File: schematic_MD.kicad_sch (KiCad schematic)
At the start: 31 parts, among them J1 XT60, J10 Gate_PWR_Jump, J11 CAN_Bus, J13 EXPWR_GND, J2 XT60, J3 XT60, J4 CAN_Bus, J5 Rotaly_encoder_1, J6 Rotaly_encoder_2, J9 Conn_02x01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

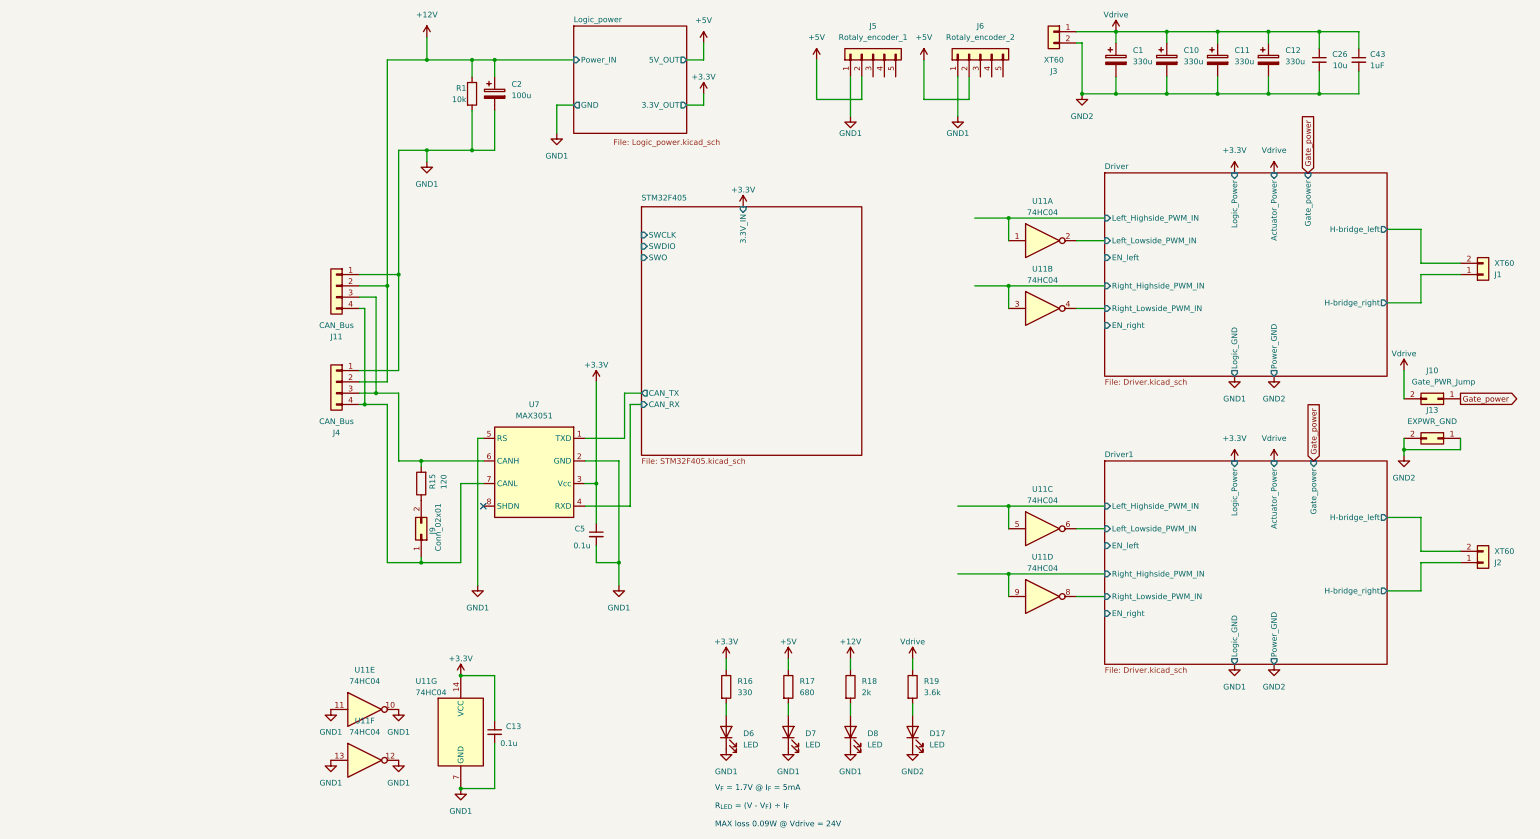
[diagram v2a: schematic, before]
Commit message: logic design update
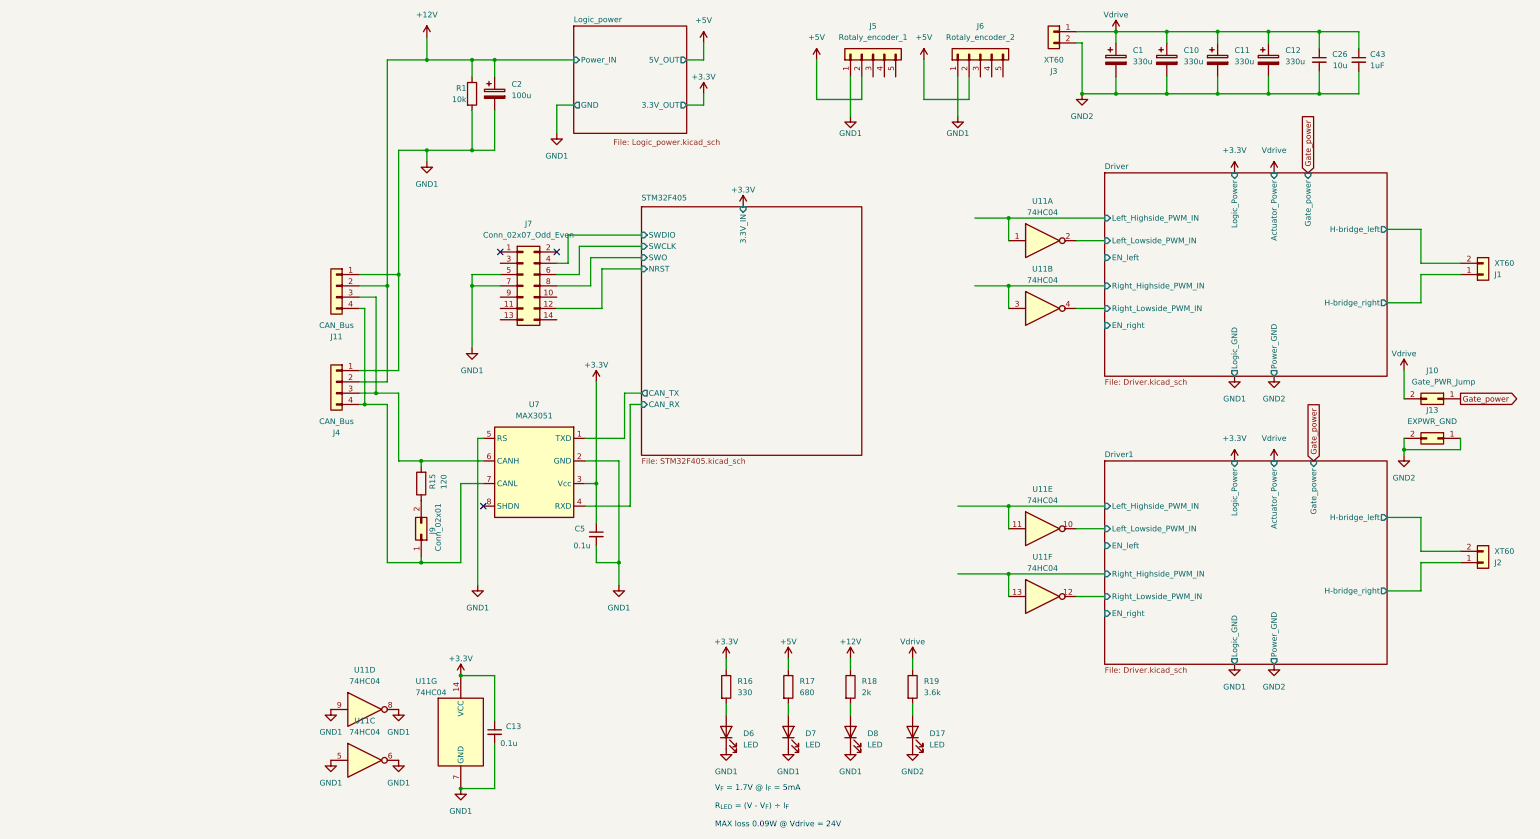
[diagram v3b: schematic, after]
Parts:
- added J7: Conn_02x07_Odd_Even, RDC_footprint:JTAG_box_connector, symbol Connector_Generic:Conn_02x07_Odd_Even
- J1, J2: footprint RDC_footprint:XT60 -> Connector_AMASS:AMASS_XT60-F_1x02_P7.20mm_Vertical
- J3: footprint RDC_footprint:XT60 -> Connector_AMASS:AMASS_XT60-M_1x02_P7.20mm_Vertical
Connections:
- net Driver1/Left_Highside_PWM_IN: now also U11.11; no longer U11.5
- net Driver1/Left_Lowside_PWM_IN: now also U11.10; no longer U11.6
- net Driver1/Right_Highside_PWM_IN: now also U11.13; no longer U11.9
- net Driver1/Right_Lowside_PWM_IN: now also U11.12; no longer U11.8
- net GND1: now also U11.5, U11.6, U11.8, U11.9, J7.5 (Pin_5), J7.7 (Pin_7); no longer U11.10, U11.11, U11.12, U11.13
- net STM32F405/SWCLK: now also J7.6 (Pin_6)
- net STM32F405/SWDIO: now also J7.4 (Pin_4)
- net STM32F405/SWO: now also J7.8 (Pin_8)
- new net STM32F405/NRST: J7.12 (Pin_12)
- no-connect marks 1 -> 3
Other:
- sheet STM32F405 ports: added NRST; removed none
- moved on the sheet: U11C, U11D, U11E, U11F

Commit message: precompleate PCB design
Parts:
- removed C43: 1uF, Capacitor_SMD:C_0603_1608Metric_Pad1.08x0.95mm_HandSolder, symbol Device:C_Small
- added H1, H2, H3, H4: MountingHole_Pad, MountingHole:MountingHole_3.2mm_M3_Pad_Via, symbol Mechanical:MountingHole_Pad
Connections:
- net GND1: now also H1.1, H2.1
- net GND2: now also H3.1, H4.1
- net STM32F405/Motor2_A: now reaches J6.3 (Pin_3)
- net STM32F405/Motor2_B: now reaches J6.4 (Pin_4)
- net STM32F405/Motor2_Z: now reaches J6.5 (Pin_5)
- net STM32F405/Motor1_A: now reaches J5.3 (Pin_3)
- net STM32F405/Motor1_B: now reaches J5.4 (Pin_4)
- net STM32F405/Motor1_Z: now reaches J5.5 (Pin_5)
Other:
- sheet STM32F405 ports: added ENABLE_1, ENABLE_2, Motor1_A, Motor1_B, Motor1_Z, Motor2_A, Motor2_B, Motor2_Z, PWM1_left, PWM1_right, PWM2_left, PWM2_right; removed none
- moved on the sheet: C1, C10, C11, C12, C26, J3, J5, J6, U11A, U11B, U11E, U11F

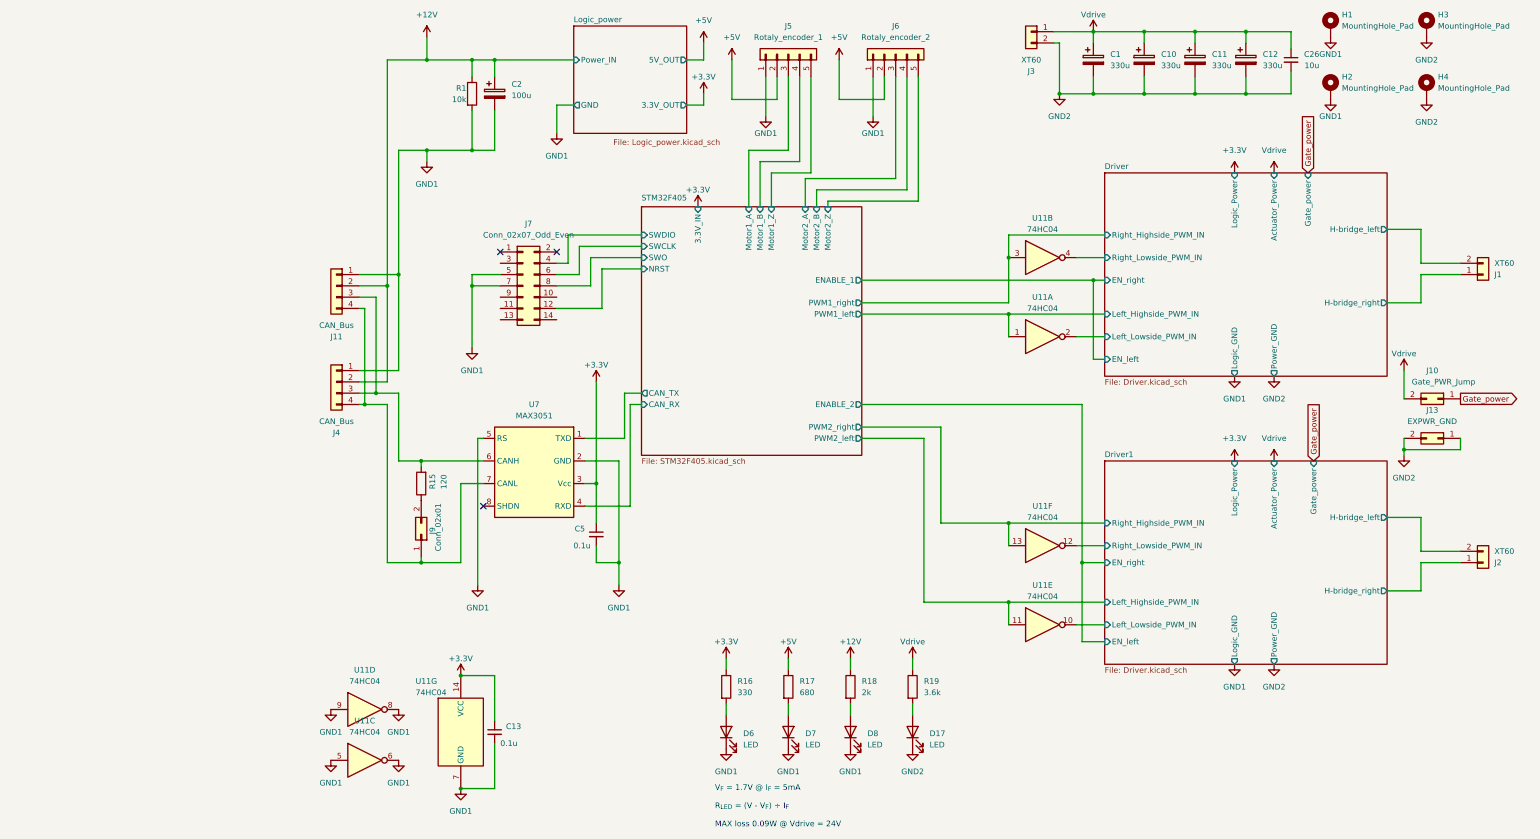
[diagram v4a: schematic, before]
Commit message: add gatedriver power
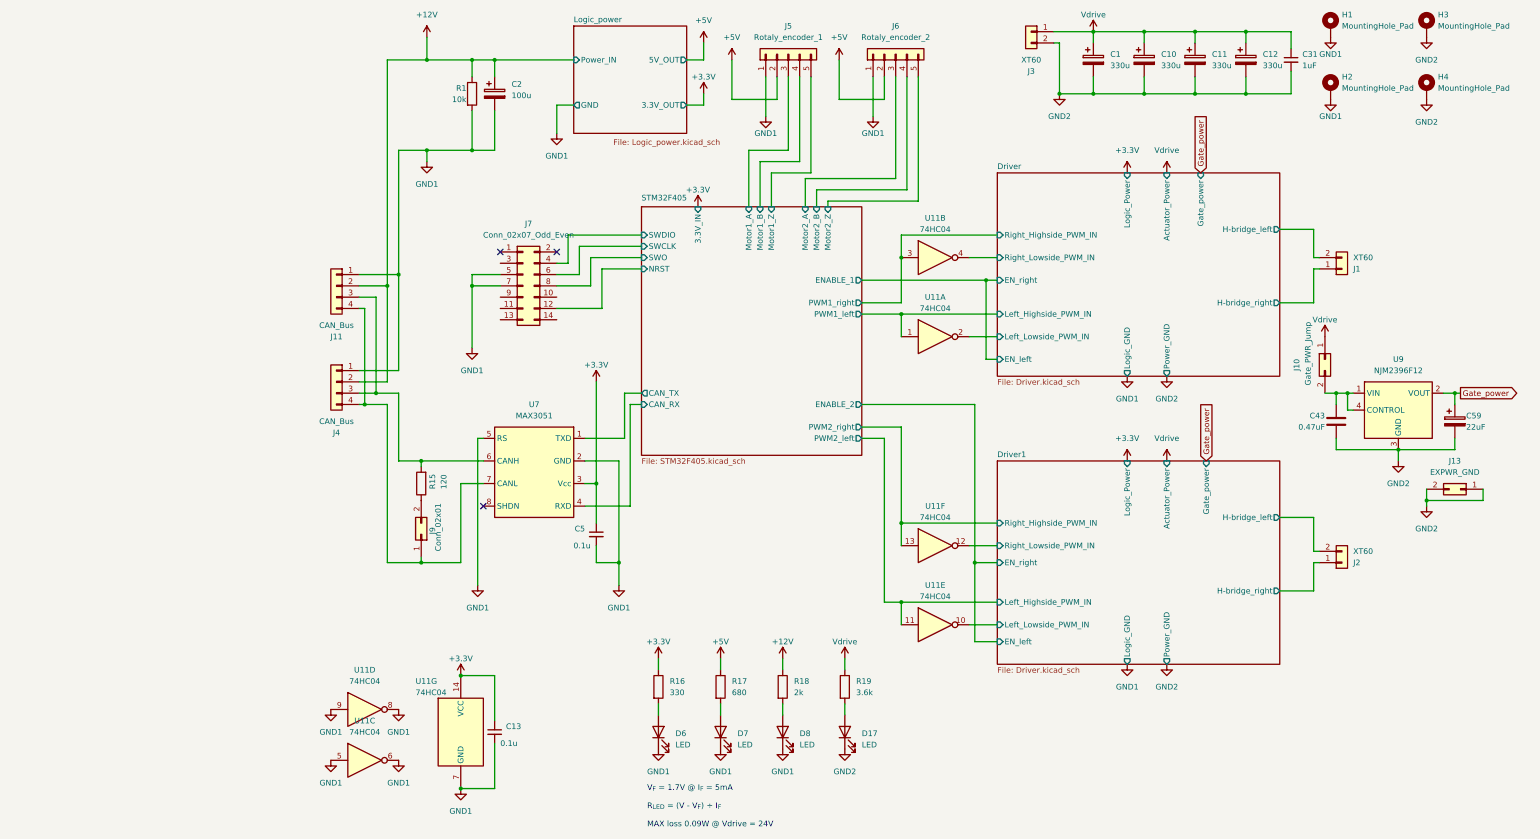
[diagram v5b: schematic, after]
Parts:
- removed C26: 10u, Capacitor_SMD:C_1210_3225Metric_Pad1.33x2.70mm_HandSolder, symbol Device:C_Small
- added C31: 1uF, Capacitor_SMD:C_0603_1608Metric_Pad1.08x0.95mm_HandSolder, symbol Device:C_Small
- added C43: 0.47uF, Capacitor_SMD:C_0805_2012Metric, symbol Device:C
- added C59: 22uF, Capacitor_THT:CP_Radial_D5.0mm_P2.00mm, symbol Device:C_Polarized
- added U9: NJM2396F12, Package_TO_SOT_THT:TO-220-4_Vertical, symbol RDC_generic:NJM2396F12
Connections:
- net GND2: now also C31.2, C43.2, C59.2, U9.3 (GND)
- net Gate_power: now also C59.1, U9.2 (VOUT); no longer J10.1 (Pin_1)
- net Vdrive: now also J10.1 (Pin_1), C31.1; no longer J10.2 (Pin_2)
- new net: C43.1, J10.2 (Pin_2), U9.1 (VIN), U9.4 (CONTROL)
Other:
- moved on the sheet: D17, D6, D7, D8, J1, J10, J13, J2, R16, R17, R18, R19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

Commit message: add silkprint & GND plane
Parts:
- added D5: D_Schottky, Diode_SMD:D_SOD-123F, symbol Device:D_Schottky
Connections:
- net Gate_power: now also D5.2 (A)
- net STM32F405/NRST: no longer J7.12 (Pin_12)
- net at C43.1, J10.2 (Pin_2), U9.1 (VIN)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: now also D5.1 (K)
- no-connect marks 3 -> 10

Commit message: release prot.1 v0.1.0
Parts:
- added C31: 1uF, Capacitor_SMD:C_0603_1608Metric_Pad1.08x0.95mm_HandSolder, symbol Device:C_Small
- added C6: 0.1u, Capacitor_SMD:C_0603_1608Metric_Pad1.08x0.95mm_HandSolder, symbol Device:C_Small
- added J8: Conn_01x04, Connector_PinHeader_2.54mm:PinHeader_1x04_P2.54mm_Vertical, symbol Connector_Generic:Conn_01x04
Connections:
- net +3.3V: now also J8.2 (Pin_2), J8.3 (Pin_3); no longer C13.1, C5.1, U11.14 (VCC), U7.3 (Vcc)
- net +5V: now also C31.2, C6.2
- net GND1: now also C31.1, C6.1
- net STM_power: now reaches J7.3 (Pin_3)
- net STM_power: now also C5.1, U7.3 (Vcc), J8.4 (Pin_4)
- new net gate_logic_PWR: C13.1, J8.1 (Pin_1), U11.14 (VCC)
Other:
- moved on the sheet: J7

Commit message: add branch v0.2.0
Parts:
- removed C43: 0.47uF, Capacitor_SMD:C_0805_2012Metric, symbol Device:C
- removed C59: 22uF, Capacitor_THT:CP_Radial_D5.0mm_P2.00mm, symbol Device:C_Polarized
- removed D5: D_Schottky, Diode_SMD:D_SOD-123F, symbol Device:D_Schottky
- removed J10: Gate_PWR_Jump, Connector_PinHeader_2.54mm:PinHeader_1x02_P2.54mm_Vertical, symbol Connector_Generic:Conn_02x01
- removed J13: EXPWR_GND, Connector_PinHeader_2.54mm:PinHeader_1x02_P2.54mm_Vertical, symbol Connector_Generic:Conn_02x01
- removed J8: Conn_01x04, Connector_PinHeader_2.54mm:PinHeader_1x04_P2.54mm_Vertical, symbol Connector_Generic:Conn_01x04
- removed U7: MAX3051, Package_TO_SOT_SMD:SOT-23-8_Handsoldering, symbol RDC_generic:MAX3051
- removed U9: NJM2396F12, Package_TO_SOT_THT:TO-220-4_Vertical, symbol RDC_generic:NJM2396F12
- added J12: Micro_SD_Card_Det2, Connector_Card:microSD_HC_Molex_47219-2001, symbol Connector:Micro_SD_Card_Det2
- added U7: MAX3051, symbol Interface_UART:MAX3051
- J1, J2: footprint Connector_AMASS:AMASS_XT60-F_1x02_P7.20mm_Vertical -> Connector_AMASS:AMASS_XT60PW-F_1x02_P7.20mm_Horizontal
- J11, J4: footprint Connector_JST:JST_XA_B04B-XASK-1_1x04_P2.50mm_Vertical -> Connector_JST:JST_XA_S04B-XASK-1_1x04_P2.50mm_Horizontal
- J3: footprint Connector_AMASS:AMASS_XT60-M_1x02_P7.20mm_Vertical -> Connector_AMASS:AMASS_XT60PW-M_1x02_P7.20mm_Horizontal
- J5, J6: footprint Connector_JST:JST_XA_B05B-XASK-1_1x05_P2.50mm_Vertical -> Connector_JST:JST_XA_S05B-XASK-1_1x05_P2.50mm_Horizontal
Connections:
- net STM_power is gone; now on net +3.3V: C5.1, J7.3 (Pin_3)
- net +3.3V: now also U7.3 (VDD)
- net GND1: now also U7.2 (GND), U7.8 (RS)
- net STM32F405/CAN_RX: now also U7.4 (RXD)
- net STM32F405/CAN_TX: now also U7.1 (TXD)
- net at J11.3 (Pin_3), J4.3 (Pin_3), R15.2: now also U7.7 (CANH)
- net at J11.4 (Pin_4), J4.4 (Pin_4), J9.1 (Pin_1): now also U7.6 (CANL)
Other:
- moved on the sheet: C5, J9, R15, U11C
